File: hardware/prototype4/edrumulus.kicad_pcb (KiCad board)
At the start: 2 copper layers, 65 x 56.5 mm, 67 parts, among them J1 Trigger Connector, J2 Raspberry Pi GPIO pins, U1 ESP32-DEVKIT-V1

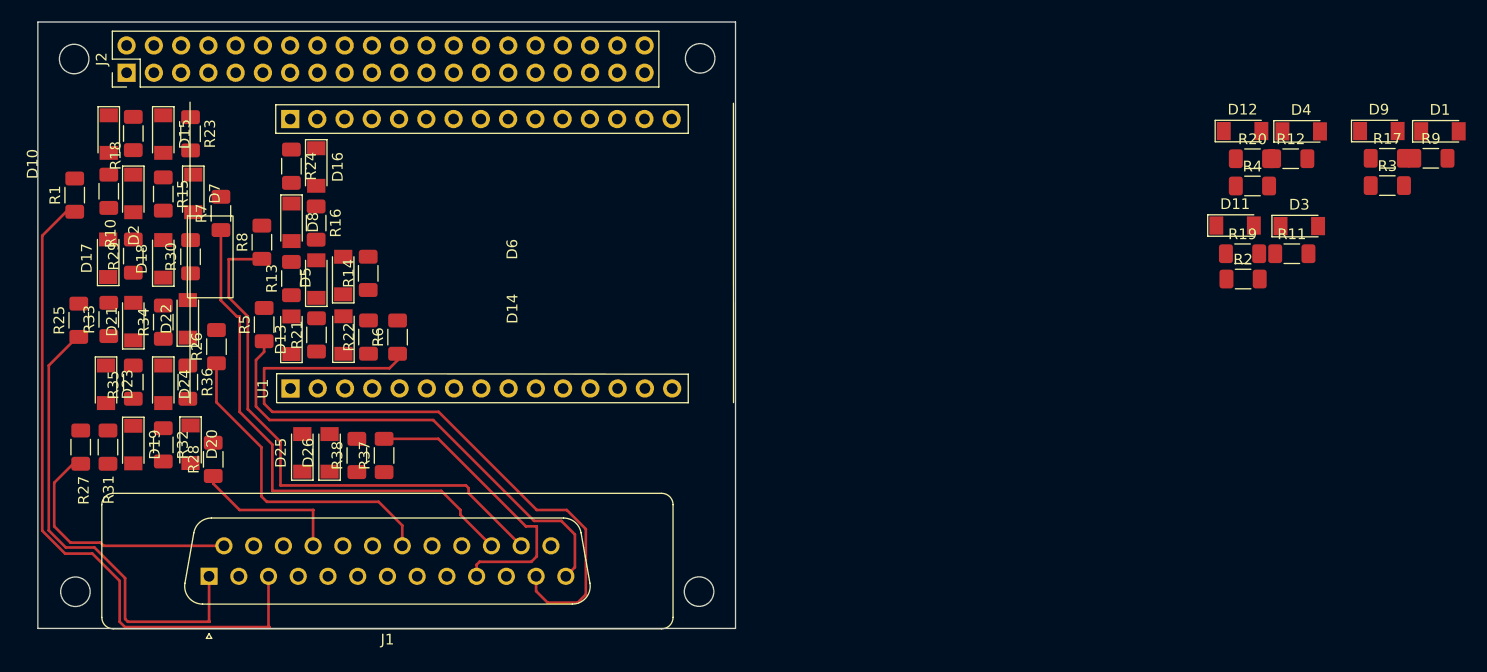
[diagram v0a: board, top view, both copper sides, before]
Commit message: finished the first routing of prototype 4
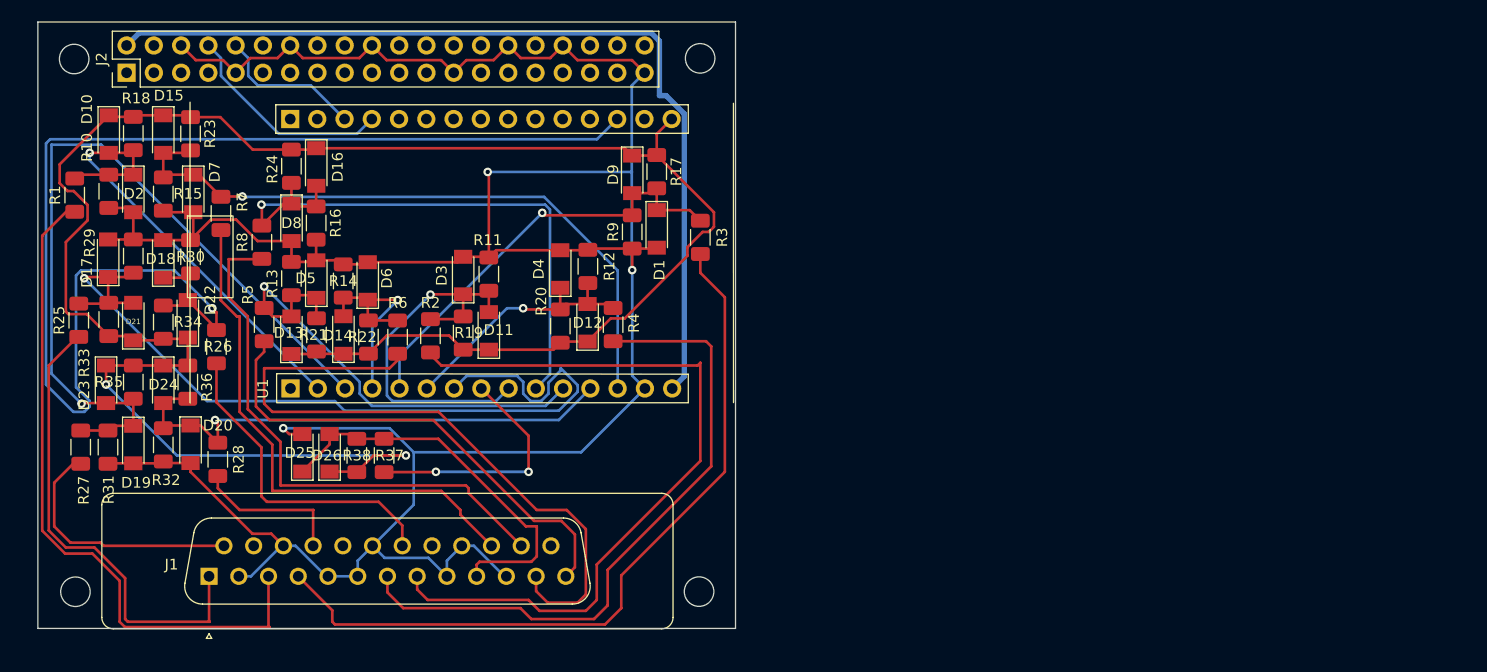
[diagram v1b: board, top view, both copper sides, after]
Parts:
- moved D3 78.0 mm to (146.3, 97.3), turned to 90 degrees
- moved R2 75.9 mm to (143.3, 102.9), turned to 90 degrees
- moved R11 74.8 mm to (148.7, 97.2), turned to 90 degrees
- moved R9 74.7 mm to (162.1, 93.2), turned to -90 degrees
- moved D1 73.5 mm to (164.3, 92.9), turned to -90 degrees
- moved R19 73.0 mm to (146.3, 102.6), turned to 90 degrees
- moved D11 70.2 mm to (148.7, 102.4), turned to 90 degrees
- moved D4 70.2 mm to (155.3, 96.7), turned to 90 degrees
- moved D9 69.7 mm to (162.1, 87.9), turned to -90 degrees
- moved R17 68.1 mm to (164.3, 87.6), turned to -90 degrees
- moved R20 66.3 mm to (155.4, 102.0), turned to 90 degrees
- moved R12 66.2 mm to (157.9, 96.4), turned to 90 degrees
- moved R3 64.2 mm to (168.4, 93.7), turned to 90 degrees
- moved D12 63.6 mm to (157.9, 101.7), turned to 90 degrees
- moved R4 61.0 mm to (160.3, 101.9), turned to 90 degrees
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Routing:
- net CRASH1-SLEEVE: track 0.00 -> 276.5 mm, vias 0 -> 3
- net 3V3: track 0.00 -> 197.5 mm, vias 0 -> 2
- net GPIO15: track 0.00 -> 122.9 mm, vias 0 -> 1
- net ESP-VIN: track 0.00 -> 84.6 mm
- net GPIO33: track 0.00 -> 81.0 mm, vias 0 -> 1
- net GPIO39: track 0.00 -> 74.7 mm, vias 0 -> 1
- net HI-HAT-RING: track 0.00 -> 71.2 mm
- net SNARE-RING: track 0.00 -> 71.1 mm
- net GPIO13: track 0.00 -> 62.1 mm, vias 0 -> 1
- net HI-HAT-TIP: track 0.00 -> 61.0 mm
- net GPIO27: track 0.00 -> 56.1 mm, vias 0 -> 1
- net GPIO12: track 0.00 -> 49.1 mm, vias 0 -> 1
- net GPIO14: track 0.00 -> 45.0 mm, vias 0 -> 1
- net GPIO36: track 0.00 -> 42.8 mm, vias 0 -> 1
- net GPIO35: track 0.00 -> 41.4 mm, vias 0 -> 1
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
